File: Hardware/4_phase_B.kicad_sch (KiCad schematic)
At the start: 17 parts

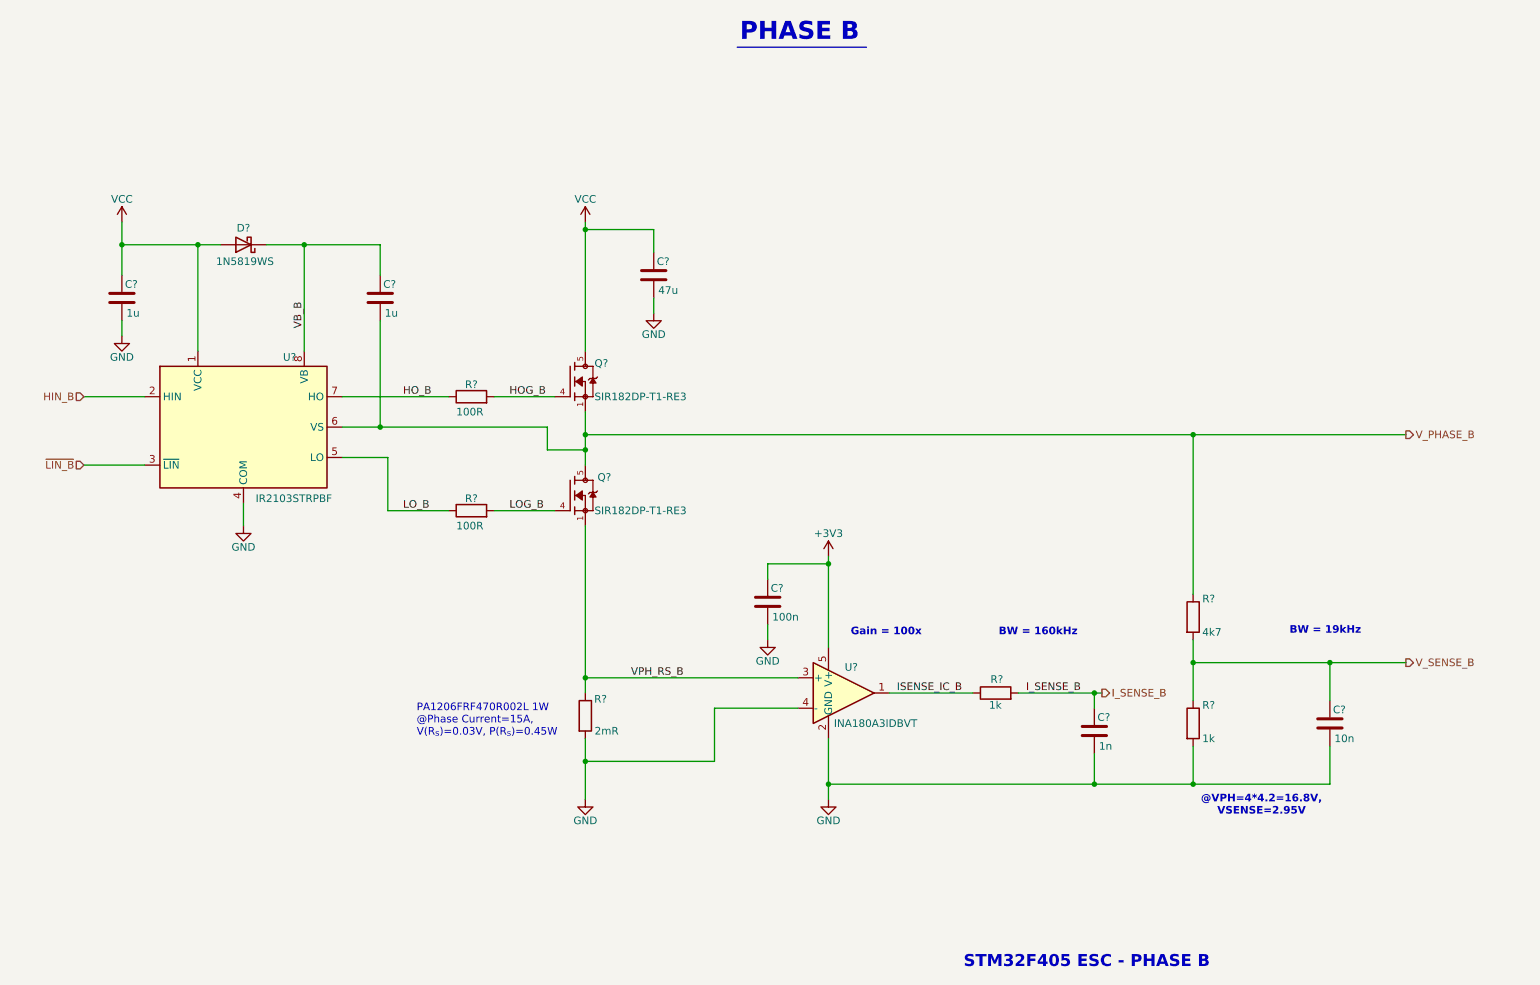
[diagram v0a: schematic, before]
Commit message: feat: Update to use I2C stemma connector
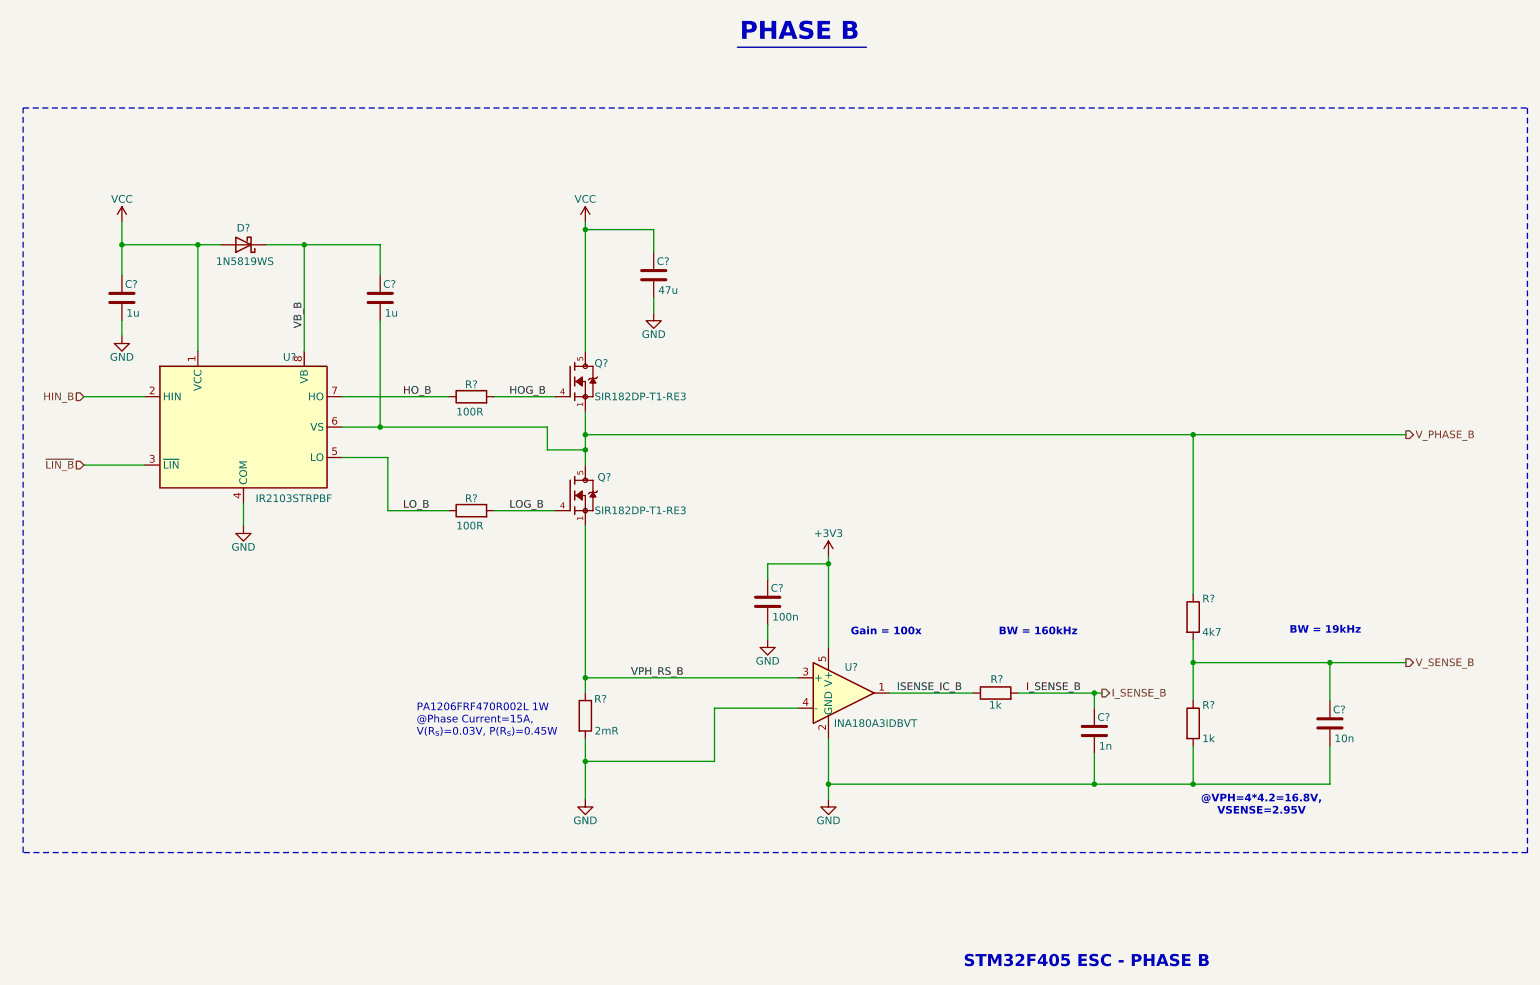
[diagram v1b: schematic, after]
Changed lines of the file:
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@@
 		(company "mangoByte")
+	)
+	(rectangle
+		(start 22.86 30.48)
+		(end 274.32 154.94)
+		(stroke
+			(width 0.2)
+			(type dash)
+		)
+		(fill
+			(type none)
+		)
 	)
 	(text "PA1206FRF470R002L 1W\n@Phase Current=15A, \nV(R_{s})=0.03V, P(R_{s})=0.45W"
